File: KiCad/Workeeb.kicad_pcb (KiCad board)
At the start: 2 copper layers, 201 parts, among them U1 Elite-C

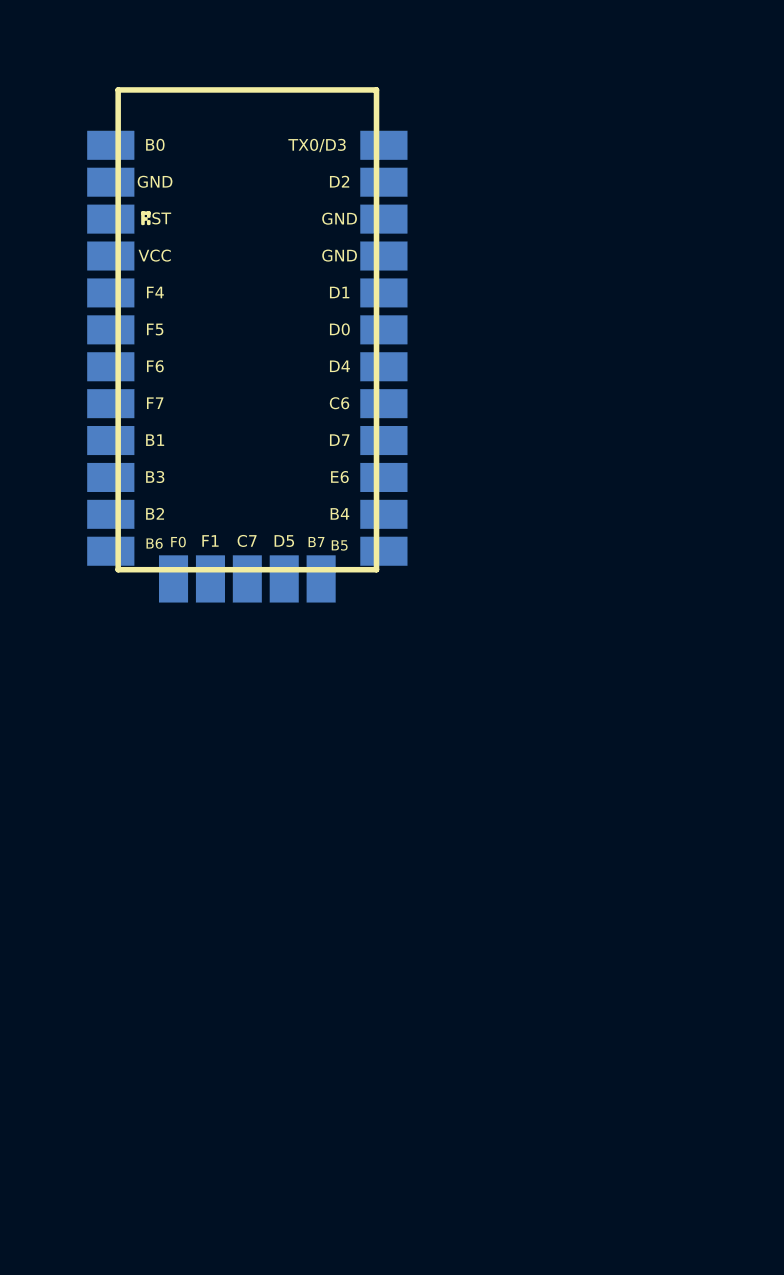
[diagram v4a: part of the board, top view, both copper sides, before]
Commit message: Add EFM32HG322F64G-C-QFP48 symbol and footprint
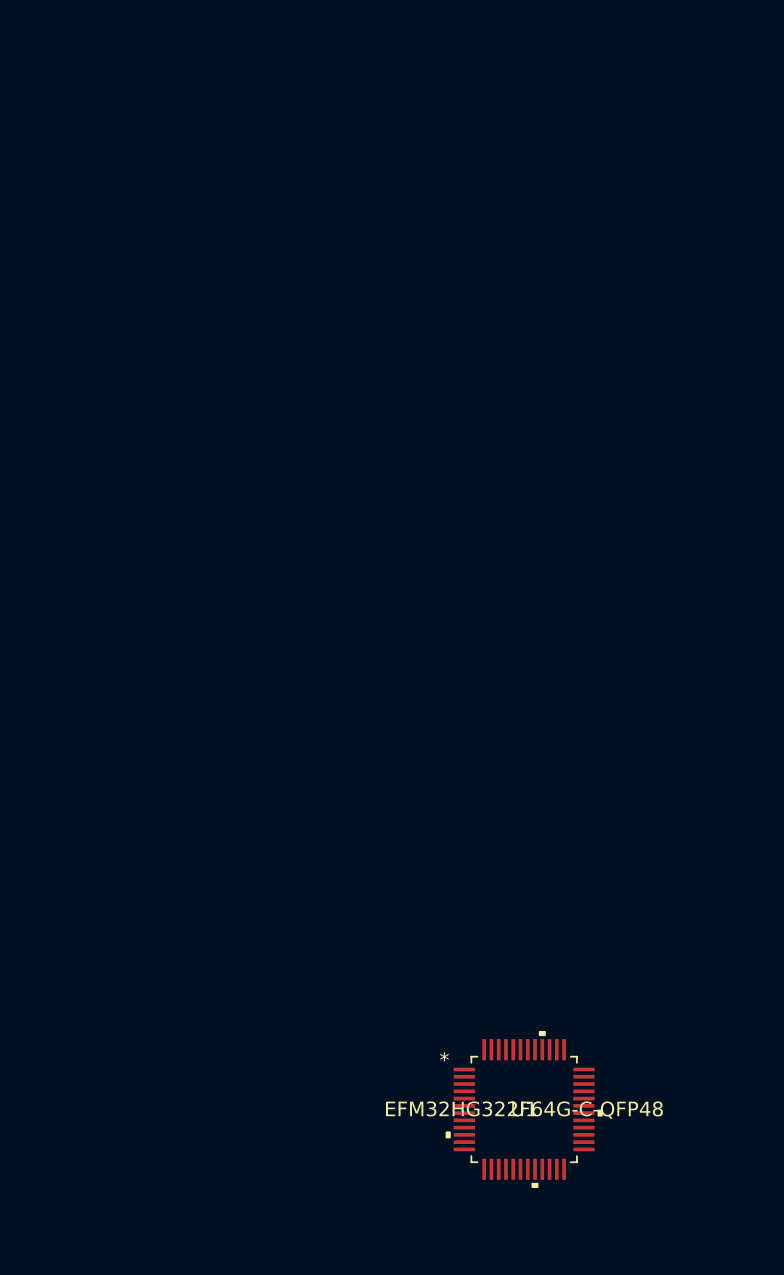
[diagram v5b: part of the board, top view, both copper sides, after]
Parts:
- U1: value Elite-C -> EFM32HG322F64G-C-QFP48; footprint Keebio-Parts:Elite-C-castellated-29pin -> EFM32HG322F64G-C-QFP48:EFM32HG322F64G-C-QFP48; moved to F.Cu
- moved U1 55.7 mm to (481.0, 85.7), turned to 0 degrees

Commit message: Begin lengthy process of hooking up switches/designing power circuitry
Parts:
- D1, D9: moved to B.Cu
- moved D1 563.3 mm to (45.2, 26.6), turned to -90 degrees
- moved D9 481.3 mm to (83.3, 26.6), turned to -90 degrees
- moved MX83 10.5 mm to (362.2, 26.2), turned to -90 degrees
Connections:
- D1 pad 1: Net-(D1-Pad1) -> ROW1
- D10 pad 1: Net-(D10-Pad1) -> ROW2
- D100 pad 1: Net-(D100-Pad1) -> ROW5
- D11 pad 1: Net-(D11-Pad1) -> ROW3
- D12 pad 1: Net-(D12-Pad1) -> ROW4
- D13 pad 1: Net-(D13-Pad1) -> ROW5
- D14 pad 1: Net-(D1-Pad1) -> ROW1
- D15 pad 1: Net-(D15-Pad1) -> ROW2
- D16 pad 1: Net-(D16-Pad1) -> ROW3
- D17 pad 1: Net-(D12-Pad1) -> ROW4
- D18 pad 1: Net-(D100-Pad1) -> ROW5
- D19 pad 1: Net-(D19-Pad1) -> ROW6
- D2 pad 1: Net-(D10-Pad1) -> ROW2
- D20 pad 1: Net-(D1-Pad1) -> ROW1
- D21 pad 1: Net-(D10-Pad1) -> ROW2
- D22 pad 1: Net-(D11-Pad1) -> ROW3
- D23 pad 1: Net-(D12-Pad1) -> ROW4
- D24 pad 1: Net-(D13-Pad1) -> ROW5
- D25 pad 1: Net-(D1-Pad1) -> ROW1
- D26 pad 1: Net-(D15-Pad1) -> ROW2
- D27 pad 1: Net-(D16-Pad1) -> ROW3
- D28 pad 1: Net-(D12-Pad1) -> ROW4
- D29 pad 1: Net-(D100-Pad1) -> ROW5
- D3 pad 1: Net-(D11-Pad1) -> ROW3
- D30 pad 1: Net-(D10-Pad1) -> ROW2
- D31 pad 1: Net-(D11-Pad1) -> ROW3
- D32 pad 1: Net-(D12-Pad1) -> ROW4
- D33 pad 1: Net-(D13-Pad1) -> ROW5
- D34 pad 1: Net-(D19-Pad1) -> ROW6
- D35 pad 1: Net-(D1-Pad1) -> ROW1
- D36 pad 1: Net-(D15-Pad1) -> ROW2
- D37 pad 1: Net-(D16-Pad1) -> ROW3
- D38 pad 1: Net-(D12-Pad1) -> ROW4
- D39 pad 1: Net-(D100-Pad1) -> ROW5
- D4 pad 1: Net-(D12-Pad1) -> ROW4
- D40 pad 1: Net-(D1-Pad1) -> ROW1
- D41 pad 1: Net-(D10-Pad1) -> ROW2
- D42 pad 1: Net-(D11-Pad1) -> ROW3
- D43 pad 1: Net-(D12-Pad1) -> ROW4
- D44 pad 1: Net-(D13-Pad1) -> ROW5
- D45 pad 1: Net-(D1-Pad1) -> ROW1
- D46 pad 1: Net-(D15-Pad1) -> ROW2
- D47 pad 1: Net-(D16-Pad1) -> ROW3
- D48 pad 1: Net-(D12-Pad1) -> ROW4
- D49 pad 1: Net-(D100-Pad1) -> ROW5
- D5 pad 1: Net-(D19-Pad1) -> ROW6
- D50 pad 1: Net-(D1-Pad1) -> ROW1
- D51 pad 1: Net-(D10-Pad1) -> ROW2
- D52 pad 1: Net-(D11-Pad1) -> ROW3
- D53 pad 1: Net-(D12-Pad1) -> ROW4
- D54 pad 1: Net-(D13-Pad1) -> ROW5
- D55 pad 1: Net-(D19-Pad1) -> ROW6
- D56 pad 1: Net-(D1-Pad1) -> ROW1
- D57 pad 1: Net-(D15-Pad1) -> ROW2
- D58 pad 1: Net-(D16-Pad1) -> ROW3
- D59 pad 1: Net-(D12-Pad1) -> ROW4
- D6 pad 1: Net-(D15-Pad1) -> ROW2
- D60 pad 1: Net-(D100-Pad1) -> ROW5
- D61 pad 1: Net-(D19-Pad1) -> ROW6
- D62 pad 1: Net-(D1-Pad1) -> ROW1
- D63 pad 1: Net-(D10-Pad1) -> ROW2
- D64 pad 1: Net-(D11-Pad1) -> ROW3
- D65 pad 1: Net-(D12-Pad1) -> ROW4
- D66 pad 1: Net-(D19-Pad1) -> ROW6
- D67 pad 1: Net-(D1-Pad1) -> ROW1
- D68 pad 1: Net-(D16-Pad1) -> ROW3
- D69 pad 1: Net-(D12-Pad1) -> ROW4
- D7 pad 1: Net-(D100-Pad1) -> ROW5
- D70 pad 1: Net-(D100-Pad1) -> ROW5
- D71 pad 1: Net-(D19-Pad1) -> ROW6
- D72 pad 1: Net-(D1-Pad1) -> ROW1
- D73 pad 1: Net-(D10-Pad1) -> ROW2
- D74 pad 1: Net-(D11-Pad1) -> ROW3
- D75 pad 1: Net-(D13-Pad1) -> ROW5
- D76 pad 1: Net-(D19-Pad1) -> ROW6
- D77 pad 1: Net-(D1-Pad1) -> ROW1
- D78 pad 1: Net-(D15-Pad1) -> ROW2
- D79 pad 1: Net-(D16-Pad1) -> ROW3
- D8 pad 1: Net-(D19-Pad1) -> ROW6
- D80 pad 1: Net-(D12-Pad1) -> ROW4
- D81 pad 1: Net-(D100-Pad1) -> ROW5
- D82 pad 1: Net-(D19-Pad1) -> ROW6
- D83 pad 1: Net-(D1-Pad1) -> ROW1
- D84 pad 1: Net-(D10-Pad1) -> ROW2
- D85 pad 1: Net-(D11-Pad1) -> ROW3
- D86 pad 1: Net-(D12-Pad1) -> ROW4
- D87 pad 1: Net-(D13-Pad1) -> ROW5
- D88 pad 1: Net-(D15-Pad1) -> ROW2
- D89 pad 1: Net-(D16-Pad1) -> ROW3
- D9 pad 1: Net-(D1-Pad1) -> ROW1
- D90 pad 1: Net-(D12-Pad1) -> ROW4
- D91 pad 1: Net-(D100-Pad1) -> ROW5
- D92 pad 1: Net-(D19-Pad1) -> ROW6
- D93 pad 1: Net-(D10-Pad1) -> ROW2
- D94 pad 1: Net-(D11-Pad1) -> ROW3
- D95 pad 1: Net-(D12-Pad1) -> ROW4
- D96 pad 1: Net-(D13-Pad1) -> ROW5
- D97 pad 1: Net-(D19-Pad1) -> ROW6
- D98 pad 1: Net-(D15-Pad1) -> ROW2
- D99 pad 1: Net-(D16-Pad1) -> ROW3
- MX1 pad 1: Net-(MX1-Pad1) -> COL1
- MX10 pad 1: Net-(MX10-Pad1) -> COL3
- MX101 pad 1: Net-(MX101-Pad1) -> COL20
- MX102 pad 1: Net-(MX101-Pad1) -> COL20
- MX103 pad 1: Net-(MX101-Pad1) -> COL20
- MX11 pad 1: Net-(MX10-Pad1) -> COL3
- MX12 pad 1: Net-(MX10-Pad1) -> COL3
- MX13 pad 1: Net-(MX10-Pad1) -> COL3
- MX14 pad 1: Net-(MX10-Pad1) -> COL4
- MX15 pad 1: Net-(MX10-Pad1) -> COL4
- MX16 pad 1: Net-(MX10-Pad1) -> COL4
- MX17 pad 1: Net-(MX10-Pad1) -> COL4
- MX18 pad 1: Net-(MX10-Pad1) -> COL4
- MX19 pad 1: Net-(MX10-Pad1) -> COL4
- MX2 pad 1: Net-(MX1-Pad1) -> COL1
- MX20 pad 1: Net-(MX20-Pad1) -> COL5
- MX21 pad 1: Net-(MX20-Pad1) -> COL5
- MX22 pad 1: Net-(MX20-Pad1) -> COL5
- MX23 pad 1: Net-(MX20-Pad1) -> COL5
- MX24 pad 1: Net-(MX20-Pad1) -> COL5
- MX25 pad 1: Net-(MX20-Pad1) -> COL6
- MX26 pad 1: Net-(MX20-Pad1) -> COL6
- MX27 pad 1: Net-(MX20-Pad1) -> COL6
- MX28 pad 1: Net-(MX20-Pad1) -> COL6
- MX29 pad 1: Net-(MX20-Pad1) -> COL6
- MX3 pad 1: Net-(MX1-Pad1) -> COL1
- MX30 pad 1: Net-(MX30-Pad1) -> COL7
- MX31 pad 1: Net-(MX30-Pad1) -> COL7
- MX32 pad 1: Net-(MX30-Pad1) -> COL7
- MX33 pad 1: Net-(MX30-Pad1) -> COL7
- MX34 pad 1: Net-(MX30-Pad1) -> COL7
- MX35 pad 1: Net-(MX30-Pad1) -> COL8
- MX36 pad 1: Net-(MX30-Pad1) -> COL8
- MX37 pad 1: Net-(MX30-Pad1) -> COL8
- MX38 pad 1: Net-(MX30-Pad1) -> COL8
- MX39 pad 1: Net-(MX30-Pad1) -> COL8
- MX4 pad 1: Net-(MX1-Pad1) -> COL1
- MX40 pad 1: Net-(MX40-Pad1) -> COL9
- MX41 pad 1: Net-(MX40-Pad1) -> COL9
- MX42 pad 1: Net-(MX40-Pad1) -> COL9
- MX43 pad 1: Net-(MX40-Pad1) -> COL9
- MX44 pad 1: Net-(MX40-Pad1) -> COL9
- MX45 pad 1: Net-(MX40-Pad1) -> COL10
- MX46 pad 1: Net-(MX40-Pad1) -> COL10
- MX47 pad 1: Net-(MX40-Pad1) -> COL10
- MX48 pad 1: Net-(MX40-Pad1) -> COL10
- MX49 pad 1: Net-(MX40-Pad1) -> COL10
- MX5 pad 1: Net-(MX1-Pad1) -> COL1
- MX50 pad 1: Net-(MX50-Pad1) -> COL11
- MX51 pad 1: Net-(MX50-Pad1) -> COL11
- MX52 pad 1: Net-(MX50-Pad1) -> COL11
- MX53 pad 1: Net-(MX50-Pad1) -> COL11
- MX54 pad 1: Net-(MX50-Pad1) -> COL11
- MX55 pad 1: Net-(MX50-Pad1) -> COL11
- MX56 pad 1: Net-(MX50-Pad1) -> COL12
- MX57 pad 1: Net-(MX50-Pad1) -> COL12
- MX58 pad 1: Net-(MX50-Pad1) -> COL12
- MX59 pad 1: Net-(MX50-Pad1) -> COL12
- MX6 pad 1: Net-(MX1-Pad1) -> COL2
- MX60 pad 1: Net-(MX50-Pad1) -> COL12
- MX61 pad 1: Net-(MX50-Pad1) -> COL12
- MX62 pad 1: Net-(MX62-Pad1) -> COL13
- MX63 pad 1: Net-(MX62-Pad1) -> COL13
- MX64 pad 1: Net-(MX62-Pad1) -> COL13
- MX65 pad 1: Net-(MX62-Pad1) -> COL13
- MX66 pad 1: Net-(MX62-Pad1) -> COL13
- MX67 pad 1: Net-(MX62-Pad1) -> COL14
- MX68 pad 1: Net-(MX62-Pad1) -> COL14
- MX69 pad 1: Net-(MX62-Pad1) -> COL14
- MX7 pad 1: Net-(MX1-Pad1) -> COL2
- MX70 pad 1: Net-(MX62-Pad1) -> COL14
- MX71 pad 1: Net-(MX62-Pad1) -> COL14
- MX72 pad 1: Net-(MX72-Pad1) -> COL15
- MX73 pad 1: Net-(MX72-Pad1) -> COL15
- MX74 pad 1: Net-(MX72-Pad1) -> COL15
- MX75 pad 1: Net-(MX72-Pad1) -> COL15
- MX76 pad 1: Net-(MX72-Pad1) -> COL15
- MX77 pad 1: Net-(MX72-Pad1) -> COL16
- MX78 pad 1: Net-(MX72-Pad1) -> COL16
- MX79 pad 1: Net-(MX72-Pad1) -> COL16
- MX8 pad 1: Net-(MX1-Pad1) -> COL2
- MX80 pad 1: Net-(MX72-Pad1) -> COL16
- MX81 pad 1: Net-(MX72-Pad1) -> COL16
- MX82 pad 1: Net-(MX72-Pad1) -> COL16
- MX83 pad S1: Net-(MX83-PadS1) -> COL17
- MX84 pad 1: Net-(MX83-PadS1) -> COL17
- MX85 pad 1: Net-(MX83-PadS1) -> COL17
- MX86 pad 1: Net-(MX83-PadS1) -> COL17
- MX87 pad 1: Net-(MX83-PadS1) -> COL17
- MX89 pad 1: Net-(MX83-PadS1) -> COL18
- MX9 pad 1: Net-(MX10-Pad1) -> COL3
- MX90 pad 1: Net-(MX83-PadS1) -> COL18
- MX91 pad 1: Net-(MX83-PadS1) -> COL18
- MX92 pad 1: Net-(MX83-PadS1) -> COL18
- MX93 pad 1: Net-(MX83-PadS1) -> COL18
- MX95 pad 1: Net-(MX101-Pad1) -> COL19
- MX96 pad 1: Net-(MX101-Pad1) -> COL19
- MX97 pad 1: Net-(MX101-Pad1) -> COL19
- MX98 pad 1: Net-(MX101-Pad1) -> COL19
- MX99 pad 1: Net-(MX101-Pad1) -> COL19
- U1 pad 1: unconnected-(U1-Pad1) -> ROW1
- U1 pad 10: unconnected-(U1-Pad10) -> COL2
- U1 pad 11: unconnected-(U1-Pad11) -> COL3
- U1 pad 12: unconnected-(U1-Pad12) -> COL4
- U1 pad 2: unconnected-(U1-Pad2) -> ROW2
- U1 pad 27: unconnected-(U1-Pad27) -> COL5
- U1 pad 3: unconnected-(U1-Pad3) -> ROW3
- U1 pad 30: unconnected-(U1-Pad30) -> COL6
- U1 pad 31: unconnected-(U1-Pad31) -> COL7
- U1 pad 32: unconnected-(U1-Pad32) -> COL8
- U1 pad 35: unconnected-(U1-Pad35) -> COL9
- U1 pad 36: unconnected-(U1-Pad36) -> COL10
- U1 pad 37: unconnected-(U1-Pad37) -> COL11
- U1 pad 38: unconnected-(U1-Pad38) -> COL12
- U1 pad 39: unconnected-(U1-Pad39) -> COL13
- U1 pad 40: unconnected-(U1-Pad40) -> COL14
- U1 pad 41: unconnected-(U1-Pad41) -> COL15
- U1 pad 42: unconnected-(U1-Pad42) -> COL16
- U1 pad 45: unconnected-(U1-Pad45) -> COL17
- U1 pad 46: unconnected-(U1-Pad46) -> COL18
- U1 pad 47: unconnected-(U1-Pad47) -> COL19
- U1 pad 48: unconnected-(U1-Pad48) -> COL20
- U1 pad 6: unconnected-(U1-Pad6) -> ROW4
- U1 pad 7: unconnected-(U1-Pad7) -> ROW5
- U1 pad 8: unconnected-(U1-Pad8) -> ROW6
- U1 pad 9: unconnected-(U1-Pad9) -> COL1
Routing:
- net ROW1: track 0.00 -> 38.1 mm
- net Net-(D9-Pad2): track 0.00 -> 6.98 mm
- net Net-(D1-Pad2): track 0.00 -> 6.98 mm

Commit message: Finish up schematic first draft
Mess around a bit with PCB
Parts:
- added C_AVDD1: 10uF, Capacitor_SMD:C_0805_2012Metric, B.Cu at (561.6, 97.0)
- added C_AVDD_0: 10nF, Capacitor_SMD:C_0805_2012Metric, B.Cu at (561.6, 94.0)
- added C_AVDD_1: 10nF, Capacitor_SMD:C_0805_2012Metric, B.Cu at (557.1, 97.0)
- added C_DEC1: 1uF, Capacitor_SMD:C_0805_2012Metric, B.Cu at (566.0, 95.5)
- added C_DEC2: 1uF, Capacitor_SMD:C_0805_2012Metric, B.Cu at (572.7, 100.1)
- added C_IOVDD1: 10uF, Capacitor_SMD:C_0805_2012Metric, B.Cu at (558.4, 91.0)
- added C_IOVDD_0: 0.1uF, Capacitor_SMD:C_0805_2012Metric, B.Cu at (557.1, 94.0)
- added C_IOVDD_3: 0.1uF, Capacitor_SMD:C_0805_2012Metric, B.Cu at (566.0, 98.5)
- added C_IOVDD_5: 0.1uF, Capacitor_SMD:C_0805_2012Metric, B.Cu at (568.2, 104.5)
- added C_RESET1: 100nF, Capacitor_SMD:C_0805_2012Metric, B.Cu at (568.2, 101.5)
- added C_VDD1: 10uF, Capacitor_SMD:C_0805_2012Metric, B.Cu at (572.7, 103.1)
- added C_VDD_1: 0.1uF, Capacitor_SMD:C_0805_2012Metric, B.Cu at (563.8, 101.5)
- added C_VREGI1: 4.7uF, Capacitor_SMD:C_0805_2012Metric, B.Cu at (549.5, 91.0)
- added C_VREGO1: 1uF, Capacitor_SMD:C_0805_2012Metric, B.Cu at (554.0, 91.0)
- added FB_VBUS1: FB, Inductor_SMD:L_0805_2012Metric, B.Cu at (563.6, 86.0)
- added J1: USB_C_Receptacle_USB2.0, Connector_USB:USB_C_Receptacle_GCT_USB4085, B.Cu at (578.0, 85.0)
- added R_CC1: 5.1k, Resistor_SMD:R_0805_2012Metric, B.Cu at (552.7, 96.9)
- added R_CC2: 5.1k, Resistor_SMD:R_0805_2012Metric, B.Cu at (552.7, 94.0)
- added R_D+1: 15, Resistor_SMD:R_0805_2012Metric, B.Cu at (559.4, 100.0)
- added R_D-1: 15, Resistor_SMD:R_0805_2012Metric, B.Cu at (563.8, 104.5)
- added R_DMPU1: 4.7K, Resistor_SMD:R_0805_2012Metric, B.Cu at (559.4, 102.9)
- added R_RESET1: 100, Resistor_SMD:R_0805_2012Metric, B.Cu at (555.0, 100.0)
- added SW_RESET1: SW_Push, random-keyboard-parts:PushButton_6x6mm_TH_Pretty, B.Cu at (583.0, 94.0)
- U1: moved to B.Cu
- turned U1 to 180 degrees
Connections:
- U1 pad 1: ROW1 -> DMPU
- U1 pad 10: COL2 -> COL1
- U1 pad 11: COL3 -> COL2
- U1 pad 12: COL4 -> COL3
- U1 pad 13: unconnected-(U1-Pad13) -> COL4
- U1 pad 16: unconnected-(U1-Pad16) -> RESET
- U1 pad 18: unconnected-(U1-Pad18) -> GND
- U1 pad 19: unconnected-(U1-Pad19) -> VDD
- U1 pad 2: ROW2 -> ROW1
- U1 pad 22: unconnected-(U1-Pad22) -> VDD
- U1 pad 23: unconnected-(U1-Pad23) -> VDD
- U1 pad 25: unconnected-(U1-Pad25) -> COL5
- U1 pad 26: unconnected-(U1-Pad26) -> COL6
- U1 pad 27: COL5 -> COL7
- U1 pad 28: unconnected-(U1-Pad28) -> VDD
- U1 pad 29: unconnected-(U1-Pad29) -> Net-(C_DEC1-Pad1)
- U1 pad 3: ROW3 -> ROW2
- U1 pad 30: COL6 -> COL8
- U1 pad 31: COL7 -> COL9
- U1 pad 32: COL8 -> COL10
- U1 pad 33: unconnected-(U1-Pad33) -> VBUS
- U1 pad 34: unconnected-(U1-Pad34) -> VDD
- U1 pad 35: COL9 -> D-
- U1 pad 36: COL10 -> D+
- U1 pad 4: unconnected-(U1-Pad4) -> VDD
- U1 pad 43: unconnected-(U1-Pad43) -> VDD
- U1 pad 44: unconnected-(U1-Pad44) -> GND
- U1 pad 5: unconnected-(U1-Pad5) -> GND
- U1 pad 6: ROW4 -> ROW3
- U1 pad 7: ROW5 -> ROW4
- U1 pad 8: ROW6 -> ROW5
- U1 pad 9: COL1 -> ROW6
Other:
- board text added: "Ferrite bead near usb c"
- board text added: "Place USB D+/- R close to MCU"

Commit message: Place all diodes and fix switch annotations
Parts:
- removed MX101: num-, MX_Only:MXOnly-1U-NoLED
- removed MX102: num+, MX_Only:MXOnly-2U-VerticalStabilizers-NoLED
- removed MX103: numEnter, MX_Only:MXOnly-2U-VerticalStabilizers-NoLED
- added MX100: numEnter, MX_Only:MXOnly-2U-VerticalStabilizers-NoLED, F.Cu at (416.7, 90.5)
- added MX88: num/, MX_Only:MXOnly-1U-NoLED, F.Cu at (378.6, 61.9)
- added MX94: num9, MX_Only:MXOnly-1U-NoLED, F.Cu at (397.7, 81.0)
- D10, D100, D11, D12, D13, D14, D15, D16, D17, D18, D19, D2, D20, D21, D22, D23, D24, D25, D26, D27, D28, D29, D3, D30, D31, D32, D33, D34, D35, D36, D37, D38, D39, D4, D40, D41, D42, D43, D44, D45, D46, D47, D48, D49, D5, D50, D51, D52, D53, D54, D55, D56, D57, D58, D59, D6, D60, D61, D62, D63, D64, D65, D66, D67, D68, D69, D7, D70, D71, D72, D73, D74, D75, D76, D77, D78, D79, D8, D80, D81, D82, D83, D84, D85, D86, D87, D88, D89, D90, D91, D92, D93, D94, D95, D96, D97, D98, D99: moved to B.Cu
- MX89: value num/ -> num8
- MX90: value num8 -> num5
- MX91: value num5 -> num2
- MX92: value num2 -> num0; footprint MX_Only:MXOnly-1U-NoLED -> MX_Only:MXOnly-2U-NoLED
- MX93: value num0 -> num*; footprint MX_Only:MXOnly-2U-NoLED -> MX_Only:MXOnly-1U-NoLED
- MX95: value num* -> num6
- MX96: value num9 -> num3
- MX97: value num6 -> num.
- MX98: value num3 -> num-
- MX99: value num. -> num+; footprint MX_Only:MXOnly-1U-NoLED -> MX_Only:MXOnly-2U-VerticalStabilizers-NoLED
- moved D5 550.5 mm to (50.0, 131.4), turned to -90 degrees
- moved D4 547.5 mm to (59.5, 93.3), turned to -90 degrees
- moved D11 535.2 mm to (73.8, 74.2), turned to -90 degrees
- moved D6 529.9 mm to (64.3, 55.2), turned to -90 degrees
- moved D13 526.8 mm to (88.1, 112.3), turned to -90 degrees
- moved D12 521.4 mm to (78.6, 93.3), turned to -90 degrees
- moved D3 519.3 mm to (54.8, 74.2), turned to -90 degrees
- moved D2 510.5 mm to (45.2, 55.2), turned to -90 degrees
- moved D10 506.8 mm to (83.3, 55.2), turned to -90 degrees
- moved D16 505.7 mm to (92.9, 74.2), turned to -90 degrees
- moved D17 504.4 mm to (97.6, 93.3), turned to -90 degrees
- moved D15 503.1 mm to (102.4, 55.2), turned to -90 degrees
- moved D22 497.1 mm to (111.9, 74.2), turned to -90 degrees
- moved D7 496.4 mm to (69.1, 112.3), turned to -90 degrees
- moved D8 494.8 mm to (73.8, 131.4), turned to -90 degrees
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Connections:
- MX89 pad 2: Net-(D88-Pad2) -> Net-(D89-Pad2)
- MX90 pad 2: Net-(D89-Pad2) -> Net-(D90-Pad2)
- MX91 pad 2: Net-(D90-Pad2) -> Net-(D91-Pad2)
- MX92 pad 2: Net-(D91-Pad2) -> Net-(D92-Pad2)
- MX93 pad 1: COL18 -> COL19
- MX93 pad 2: Net-(D92-Pad2) -> Net-(D93-Pad2)
- MX95 pad 2: Net-(D93-Pad2) -> Net-(D95-Pad2)
- MX96 pad 2: Net-(D94-Pad2) -> Net-(D96-Pad2)
- MX97 pad 2: Net-(D95-Pad2) -> Net-(D97-Pad2)
- MX98 pad 1: COL19 -> COL20
- MX98 pad 2: Net-(D96-Pad2) -> Net-(D98-Pad2)
- MX99 pad 1: COL19 -> COL20
- MX99 pad 2: Net-(D97-Pad2) -> Net-(D99-Pad2)
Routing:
- net ROW1: track 38.1 -> 295.2 mm
- net ROW3: track 0.00 -> 47.5 mm
- net Net-(D74-Pad2): track 0.00 -> 11.7 mm
- net Net-(D68-Pad2): track 0.00 -> 6.93 mm
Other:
- board text added: "All dcoupling caps near VDD source"
- board text added: "Check screw clearance of D86"
